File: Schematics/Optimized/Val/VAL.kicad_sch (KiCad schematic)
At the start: 2 parts

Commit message: Polish
Tested: passed expmon_test_{typ,val} (-busmux)
Tested: passed run_udiag on r2000
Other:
- removed sheet Page 14
- removed sheet Page 20
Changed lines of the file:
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@@
-    )
-  )
-  (sheet (at 12.7 165.1) (size 20.32 5.08)
-    (stroke (width 0) (type solid))
-    (fill (color 0 0 0 0.0000))
-    (property "Sheetname" "Page 20" (at 35.56 170.18 0)
-      (effects (font (size 2.54 2.54)) (justify left bottom))
-    )
-    (property "Sheetfile" "pg_20.kicad_sch" (at 35.56 167.64 0)
-      (effects (font (size 1.27 1.27)) (justify left bottom) hide)
-    )
-    (instances
-      (project "VAL"
-        (path "/20011966-0b12-5e7d-4f5d-7b7451992361" (page "20"))
-      )
     )
   )
@@
       )
     )
-  )
-  (sheet (at 12.7 119.38) (size 20.32 5.08)
-    (stroke (width 0) (type solid))
-    (fill (color 0 0 0 0.0000))
-    (property "Sheetname" "Page 14" (at 35.56 124.46 0)
-      (effects (font (size 2.54 2.54)) (justify left bottom))
-    )
-    (property "Sheetfile" "pg_14.kicad_sch" (at 35.56 121.92 0)
-      (effects (font (size 1.27 1.27)) (justify left bottom) hide)
-    )
-    (instances
-      (project "VAL"
-        (path "/20011966-0b12-5e7d-4f5d-7b7451992361" (page "14"))
-      )
-    )

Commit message: TYP+VAL condensation
Tested: passed expmon_test_val (-muxbus)
Tested: passed expmon_test_typ (-muxbus)
Tested: passed run_udiag
Tested: passed boot_env (R2_INTEG until PRETTY_PRINTER)
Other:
- removed sheet Page 49
- removed sheet Page 50
- removed sheet Page 59
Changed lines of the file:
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@@
-    )
-  )
-  (sheet (at 266.7 50.8) (size 20.32 5.08)
-    (stroke (width 0) (type solid))
-    (fill (color 0 0 0 0.0000))
-    (property "Sheetname" "Page 50" (at 289.56 55.88 0)
-      (effects (font (size 2.54 2.54)) (justify left bottom))
-    )
-    (property "Sheetfile" "pg_50.kicad_sch" (at 289.56 53.34 0)
-      (effects (font (size 1.27 1.27)) (justify left bottom) hide)
-    )
-    (instances
-      (project "VAL"
-        (path "/20011966-0b12-5e7d-4f5d-7b7451992361" (page "50"))
-      )
     )
   )
@@
     )
   )
-  (sheet (at 266.7 119.38) (size 20.32 5.08)
-    (stroke (width 0) (type solid))
-    (fill (color 0 0 0 0.0000))
-    (property "Sheetname" "Page 59" (at 289.56 124.46 0)
-      (effects (font (size 2.54 2.54)) (justify left bottom))
-    )
-    (property "Sheetfile" "pg_59.kicad_sch" (at 289.56 121.92 0)
-      (effects (font (size 1.27 1.27)) (justify left bottom) hide)
-    )
-    (instances
-      (project "VAL"
-        (path "/20011966-0b12-5e7d-4f5d-7b7451992361" (page "59"))
-      )
-    )
-  )
   (sheet (at 266.7 149.86) (size 20.32 5.08)
     (stroke (width 0) (type solid))
@@
       )
     )
-  )
-  (sheet (at 266.7 43.18) (size 20.32 5.08)
-    (stroke (width 0) (type solid))
-    (fill (color 0 0 0 0.0000))
-    (property "Sheetname" "Page 49" (at 289.56 48.26 0)
-      (effects (font (size 2.54 2.54)) (justify left bottom))
-    )
-    (property "Sheetfile" "pg_49.kicad_sch" (at 289.56 45.72 0)
-      (effects (font (size 1.27 1.27)) (justify left bottom) hide)
-    )
-    (instances
-      (project "VAL"
-        (path "/20011966-0b12-5e7d-4f5d-7b7451992361" (page "49"))
-      )
-    )

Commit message: Integrate R2_TV (mainly state clock)
Tested: passed run_udiag
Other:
- removed sheet Page 63
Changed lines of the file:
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@@
-    )
-  )
-  (sheet (at 266.7 149.86) (size 20.32 5.08)
-    (stroke (width 0) (type solid))
-    (fill (color 0 0 0 0.0000))
-    (property "Sheetname" "Page 63" (at 289.56 154.94 0)
-      (effects (font (size 2.54 2.54)) (justify left bottom))
-    )
-    (property "Sheetfile" "pg_63.kicad_sch" (at 289.56 152.4 0)
-      (effects (font (size 1.27 1.27)) (justify left bottom) hide)
-    )
-    (instances
-      (project "VAL"
-        (path "/20011966-0b12-5e7d-4f5d-7b7451992361" (page "63"))
-      )
     )
   )

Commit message: Optimization of TYP & VAL
Tested: boot_env (until PRETTY_PRINTER assert)
Tested: passed run_udiag
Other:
- removed sheet Page 22
- removed sheet Page 24
- removed sheet Page 36
- removed sheet Page 39
- removed sheet Page 57
- removed sheet Page 58
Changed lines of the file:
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@@
-    )
-  )
-  (sheet (at 12.7 195.58) (size 20.32 5.08)
-    (stroke (width 0) (type solid))
-    (fill (color 0 0 0 0.0000))
-    (property "Sheetname" "Page 24" (at 35.56 200.66 0)
-      (effects (font (size 2.54 2.54)) (justify left bottom))
-    )
-    (property "Sheetfile" "pg_24.kicad_sch" (at 35.56 198.12 0)
-      (effects (font (size 1.27 1.27)) (justify left bottom) hide)
-    )
-    (instances
-      (project "VAL"
-        (path "/20011966-0b12-5e7d-4f5d-7b7451992361" (page "24"))
-      )
     )
   )
@@
     )
   )
-  (sheet (at 12.7 180.34) (size 20.32 5.08)
-    (stroke (width 0) (type solid))
-    (fill (color 0 0 0 0.0000))
-    (property "Sheetname" "Page 22" (at 35.56 185.42 0)
-      (effects (font (size 2.54 2.54)) (justify left bottom))
-    )
-    (property "Sheetfile" "pg_22.kicad_sch" (at 35.56 182.88 0)
-      (effects (font (size 1.27 1.27)) (justify left bottom) hide)
-    )
-    (instances
-      (project "VAL"
-        (path "/20011966-0b12-5e7d-4f5d-7b7451992361" (page "22"))
-      )
-    )
-  )
   (sheet (at 266.7 27.94) (size 20.32 5.08)
     (stroke (width 0) (type solid))
@@
     )
   )
-  (sheet (at 12.7 287.02) (size 20.32 5.08)
-    (stroke (width 0) (type solid))
-    (fill (color 0 0 0 0.0000))
-    (property "Sheetname" "Page 36" (at 35.56 292.1 0)
-      (effects (font (size 2.54 2.54)) (justify left bottom))
-    )
-    (property "Sheetfile" "pg_36.kicad_sch" (at 35.56 289.56 0)
-      (effects (font (size 1.27 1.27)) (justify left bottom) hide)
-    )
-    (instances
-      (project "VAL"
-        (path "/20011966-0b12-5e7d-4f5d-7b7451992361" (page "36"))
-      )
-    )
-  )
-  (sheet (at 266.7 104.14) (size 20.32 5.08)
-    (stroke (width 0) (type solid))
-    (fill (color 0 0 0 0.0000))
-    (property "Sheetname" "Page 57" (at 289.56 109.22 0)
-      (effects (font (size 2.54 2.54)) (justify left bottom))
-    )
-    (property "Sheetfile" "pg_57.kicad_sch" (at 289.56 106.68 0)
-      (effects (font (size 1.27 1.27)) (justify left bottom) hide)
-    )
-    (instances
-      (project "VAL"
-        (path "/20011966-0b12-5e7d-4f5d-7b7451992361" (page "57"))
-      )
-    )
-  )
   (sheet (at 12.7 294.64) (size 20.32 5.08)
     (stroke (width 0) (type solid))
@@
       )
     )
-  )
-  (sheet (at 12.7 309.88) (size 20.32 5.08)
-    (stroke (width 0) (type solid))
-    (fill (color 0 0 0 0.0000))
-    (property "Sheetname" "Page 39" (at 35.56 314.96 0)
-      (effects (font (size 2.54 2.54)) (justify left bottom))
-    )
-    (property "Sheetfile" "pg_39.kicad_sch" (at 35.56 312.42 0)
-      (effects (font (size 1.27 1.27)) (justify left bottom) hide)
-    )
-    (instances
-      (project "VAL"
-        (path "/20011966-0b12-5e7d-4f5d-7b7451992361" (page "39"))
-      )
-    )
-  )
-  (sheet (at 266.7 111.76) (size 20.32 5.08)
-    (stroke (width 0) (type solid))
-    (fill (color 0 0 0 0.0000))
-    (property "Sheetname" "Page 58" (at 289.56 116.84 0)
-      (effects (font (size 2.54 2.54)) (justify left bottom))
-    )
-    (property "Sheetfile" "pg_58.kicad_sch" (at 289.56 114.3 0)
-      (effects (font (size 1.27 1.27)) (justify left bottom) hide)
-    )
-    (instances
-      (project "VAL"
-        (path "/20011966-0b12-5e7d-4f5d-7b7451992361" (page "58"))
-      )
-    )

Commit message: TYP+VAL: Condensation, mostly Register File
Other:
- removed sheet Page 17
- removed sheet Page 37
- removed sheet Page 38
- removed sheet Page 47
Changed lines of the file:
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@@
-    )
-  )
-  (sheet (at 12.7 302.26) (size 20.32 5.08)
-    (stroke (width 0) (type solid))
-    (fill (color 0 0 0 0.0000))
-    (property "Sheetname" "Page 38" (at 35.56 307.34 0)
-      (effects (font (size 2.54 2.54)) (justify left bottom))
-    )
-    (property "Sheetfile" "pg_38.kicad_sch" (at 35.56 304.8 0)
-      (effects (font (size 1.27 1.27)) (justify left bottom) hide)
-    )
-    (instances
-      (project "VAL"
-        (path "/20011966-0b12-5e7d-4f5d-7b7451992361" (page "38"))
-      )
     )
   )
@@
     )
   )
-  (sheet (at 266.7 27.94) (size 20.32 5.08)
-    (stroke (width 0) (type solid))
-    (fill (color 0 0 0 0.0000))
-    (property "Sheetname" "Page 47" (at 289.56 33.02 0)
-      (effects (font (size 2.54 2.54)) (justify left bottom))
-    )
-    (property "Sheetfile" "pg_47.kicad_sch" (at 289.56 30.48 0)
-      (effects (font (size 1.27 1.27)) (justify left bottom) hide)
-    )
-    (instances
-      (project "VAL"
-        (path "/20011966-0b12-5e7d-4f5d-7b7451992361" (page "47"))
-      )
-    )
-  )
   (sheet (at 12.7 134.62) (size 20.32 5.08)
     (stroke (width 0) (type solid))
@@
     )
   )
-  (sheet (at 12.7 294.64) (size 20.32 5.08)
-    (stroke (width 0) (type solid))
-    (fill (color 0 0 0 0.0000))
-    (property "Sheetname" "Page 37" (at 35.56 299.72 0)
-      (effects (font (size 2.54 2.54)) (justify left bottom))
-    )
-    (property "Sheetfile" "pg_37.kicad_sch" (at 35.56 297.18 0)
-      (effects (font (size 1.27 1.27)) (justify left bottom) hide)
-    )
-    (instances
-      (project "VAL"
-        (path "/20011966-0b12-5e7d-4f5d-7b7451992361" (page "37"))
-      )
-    )
-  )
   (sheet (at 12.7 157.48) (size 20.32 5.08)
     (stroke (width 0) (type solid))
@@
       )
     )
-  )
-  (sheet (at 12.7 142.24) (size 20.32 5.08)
-    (stroke (width 0) (type solid))
-    (fill (color 0 0 0 0.0000))
-    (property "Sheetname" "Page 17" (at 35.56 147.32 0)
-      (effects (font (size 2.54 2.54)) (justify left bottom))
-    )
-    (property "Sheetfile" "pg_17.kicad_sch" (at 35.56 144.78 0)
-      (effects (font (size 1.27 1.27)) (justify left bottom) hide)
-    )
-    (instances
-      (project "VAL"
-        (path "/20011966-0b12-5e7d-4f5d-7b7451992361" (page "17"))
-      )
-    )

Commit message: TYP/VAL Register File condensation
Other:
- removed sheet Page 18
- removed sheet Page 23
- removed sheet Page 48
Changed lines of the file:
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@@
-    )
-  )
-  (sheet (at 266.7 35.56) (size 20.32 5.08)
-    (stroke (width 0) (type solid))
-    (fill (color 0 0 0 0.0000))
-    (property "Sheetname" "Page 48" (at 289.56 40.64 0)
-      (effects (font (size 2.54 2.54)) (justify left bottom))
-    )
-    (property "Sheetfile" "pg_48.kicad_sch" (at 289.56 38.1 0)
-      (effects (font (size 1.27 1.27)) (justify left bottom) hide)
-    )
-    (instances
-      (project "VAL"
-        (path "/20011966-0b12-5e7d-4f5d-7b7451992361" (page "48"))
-      )
     )
   )
@@
     )
   )
-  (sheet (at 12.7 149.86) (size 20.32 5.08)
-    (stroke (width 0) (type solid))
-    (fill (color 0 0 0 0.0000))
-    (property "Sheetname" "Page 18" (at 35.56 154.94 0)
-      (effects (font (size 2.54 2.54)) (justify left bottom))
-    )
-    (property "Sheetfile" "pg_18.kicad_sch" (at 35.56 152.4 0)
-      (effects (font (size 1.27 1.27)) (justify left bottom) hide)
-    )
-    (instances
-      (project "VAL"
-        (path "/20011966-0b12-5e7d-4f5d-7b7451992361" (page "18"))
-      )
-    )
-  )
   (sheet (at 266.7 73.66) (size 20.32 5.08)
     (stroke (width 0) (type solid))
@@
       )
     )
-  )
-  (sheet (at 12.7 187.96) (size 20.32 5.08)
-    (stroke (width 0) (type solid))
-    (fill (color 0 0 0 0.0000))
-    (property "Sheetname" "Page 23" (at 35.56 193.04 0)
-      (effects (font (size 2.54 2.54)) (justify left bottom))
-    )
-    (property "Sheetfile" "pg_23.kicad_sch" (at 35.56 190.5 0)
-      (effects (font (size 1.27 1.27)) (justify left bottom) hide)
-    )
-    (instances
-      (project "VAL"
-        (path "/20011966-0b12-5e7d-4f5d-7b7451992361" (page "23"))
-      )
-    )

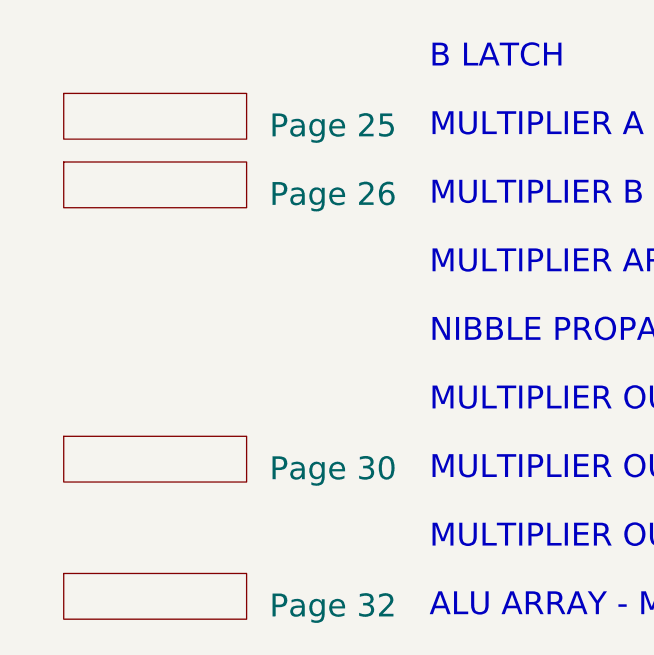
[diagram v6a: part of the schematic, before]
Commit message: Speedup: Condense multiplier, clocked parity comparison and more.
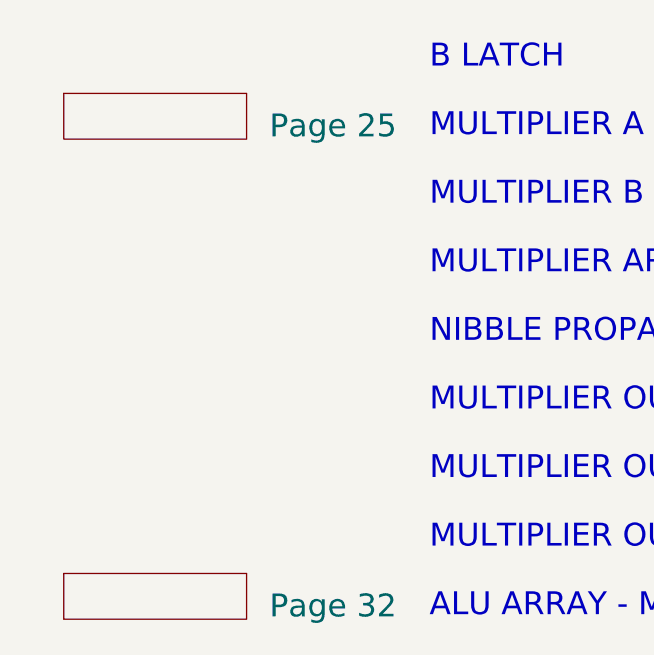
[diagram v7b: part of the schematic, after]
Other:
- removed sheet Page 26
- removed sheet Page 30
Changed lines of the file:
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@@
-    )
-  )
-  (sheet (at 12.7 210.82) (size 20.32 5.08)
-    (stroke (width 0) (type solid))
-    (fill (color 0 0 0 0.0000))
-    (property "Sheetname" "Page 26" (at 35.56 215.9 0)
-      (effects (font (size 2.54 2.54)) (justify left bottom))
-    )
-    (property "Sheetfile" "pg_26.kicad_sch" (at 35.56 213.36 0)
-      (effects (font (size 1.27 1.27)) (justify left bottom) hide)
-    )
-    (instances
-      (project "VAL"
-        (path "/20011966-0b12-5e7d-4f5d-7b7451992361" (page "26"))
-      )
     )
   )
@@
       )
     )
-  )
-  (sheet (at 12.7 241.3) (size 20.32 5.08)
-    (stroke (width 0) (type solid))
-    (fill (color 0 0 0 0.0000))
-    (property "Sheetname" "Page 30" (at 35.56 246.38 0)
-      (effects (font (size 2.54 2.54)) (justify left bottom))
-    )
-    (property "Sheetfile" "pg_30.kicad_sch" (at 35.56 243.84 0)
-      (effects (font (size 1.27 1.27)) (justify left bottom) hide)
-    )
-    (instances
-      (project "VAL"
-        (path "/20011966-0b12-5e7d-4f5d-7b7451992361" (page "30"))
-      )
-    )

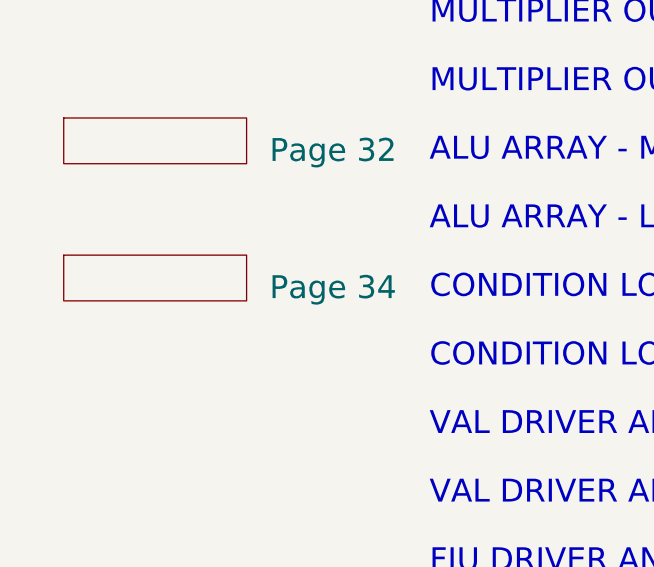
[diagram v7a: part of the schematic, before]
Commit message: Condensation of SEQ, TYP & VAL conditions
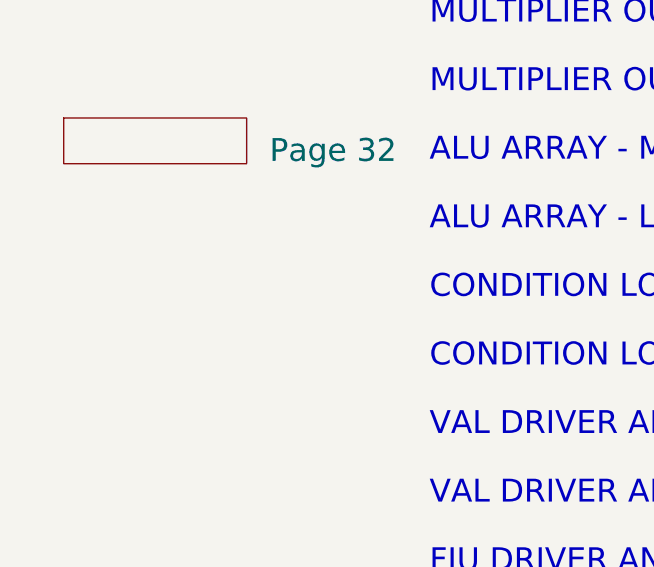
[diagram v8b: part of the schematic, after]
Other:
- removed sheet Page 34
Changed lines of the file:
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@@
-    )
-  )
-  (sheet (at 12.7 271.78) (size 20.32 5.08)
-    (stroke (width 0) (type solid))
-    (fill (color 0 0 0 0.0000))
-    (property "Sheetname" "Page 34" (at 35.56 276.86 0)
-      (effects (font (size 2.54 2.54)) (justify left bottom))
-    )
-    (property "Sheetfile" "pg_34.kicad_sch" (at 35.56 274.32 0)
-      (effects (font (size 1.27 1.27)) (justify left bottom) hide)
-    )
-    (instances
-      (project "VAL"
-        (path "/20011966-0b12-5e7d-4f5d-7b7451992361" (page "34"))
-      )
     )
   )
